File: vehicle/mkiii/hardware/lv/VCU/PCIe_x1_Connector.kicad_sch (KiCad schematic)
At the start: 15 parts, among them J2 J_PCIe_x1, U13 MCP6001T-I/LT

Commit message: Resolved some "footprint not exist" issues
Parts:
- J2: footprint OEM:J_PCIe_x1 -> OEM:J_PCIe_x1_Key
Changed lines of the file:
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@@
 			)
 		)
-		(property "Footprint" "OEM:J_PCIe_x1"
+		(property "Footprint" "OEM:J_PCIe_x1_Key"
 			(at 170.18 77.47 0)
 			(effects

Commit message: Layout completed, review required
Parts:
- renumbered C9 to C12, C30 to C13, C27 to C14, R45 to R11, R46 to R12, R42 to R13, R47 to R14, R48 to R15, R44 to R16, R43 to R17, U13 to U3
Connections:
- no-connect marks 15 -> 17
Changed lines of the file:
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@@
 	)
 	(no_connect
+		(at 187.96 134.62)
+	)
+	(no_connect
 		(at 190.5 91.44)
 	)
@@
 	)
 	(no_connect
+		(at 152.4 88.9)
+	)
+	(no_connect
 		(at 190.5 116.84)
 	)
@@
 		(dnp no)
 		(fields_autoplaced yes)
-		(property "Reference" "R42"
+		(property "Reference" "R13"
 			(at 203.2 38.0999 0)
 			(effects
@@
 			(project "VCU"
 				(path "/ec5dd9e3-3092-4af4-bee1-94131d9ab7f8/f5075997-e0a3-4d84-b3da-8739948f4d50"
-					(reference "R42")
+					(reference "R13")
 					(unit 1)
 				)
@@
 		(dnp no)
 		(fields_autoplaced yes)
-		(property "Reference" "R46"
+		(property "Reference" "R12"
 			(at 143.51 175.2599 0)
 			(effects
@@
 			(project "VCU"
 				(path "/ec5dd9e3-3092-4af4-bee1-94131d9ab7f8/f5075997-e0a3-4d84-b3da-8739948f4d50"
-					(reference "R46")
+					(reference "R12")
 					(unit 1)
 				)
@@
 		(dnp no)
 		(fields_autoplaced yes)
-		(property "Reference" "C27"
+		(property "Reference" "C14"
 			(at 213.36 29.21 90)
 			(effects
@@
 			(project "VCU"
 				(path "/ec5dd9e3-3092-4af4-bee1-94131d9ab7f8/f5075997-e0a3-4d84-b3da-8739948f4d50"
-					(reference "C27")
+					(reference "C14")
 					(unit 1)
 				)
@@
 		(dnp no)
 		(fields_autoplaced yes)
-		(property "Reference" "R48"
+		(property "Reference" "R15"
 			(at 220.98 90.1699 0)
 			(effects
@@
 			(project "VCU"
 				(path "/ec5dd9e3-3092-4af4-bee1-94131d9ab7f8/f5075997-e0a3-4d84-b3da-8739948f4d50"
-					(reference "R48")
+					(reference "R15")
 					(unit 1)
 				)
@@
 		(dnp no)
 		(fields_autoplaced yes)
-		(property "Reference" "C9"
+		(property "Reference" "C12"
 			(at 135.89 63.4999 0)
 			(effects
@@
 			(project ""
 				(path "/ec5dd9e3-3092-4af4-bee1-94131d9ab7f8/f5075997-e0a3-4d84-b3da-8739948f4d50"
-					(reference "C9")
+					(reference "C12")
 					(unit 1)
 				)
@@
 		(on_board yes)
 		(dnp no)
-		(property "Reference" "R44"
+		(property "Reference" "R16"
 			(at 236.22 63.4999 0)
 			(effects
@@
 			(project "VCU"
 				(path "/ec5dd9e3-3092-4af4-bee1-94131d9ab7f8/f5075997-e0a3-4d84-b3da-8739948f4d50"
-					(reference "R44")
+					(reference "R16")
 					(unit 1)
 				)
@@
 		(dnp no)
 		(fields_autoplaced yes)
-		(property "Reference" "C30"
+		(property "Reference" "C13"
 			(at 137.16 86.3599 0)
 			(effects
@@
 			(project "VCU"
 				(path "/ec5dd9e3-3092-4af4-bee1-94131d9ab7f8/f5075997-e0a3-4d84-b3da-8739948f4d50"
-					(reference "C30")
+					(reference "C13")
 					(unit 1)
 				)
@@
 		(dnp no)
 		(fields_autoplaced yes)
-		(property "Reference" "U13"
+		(property "Reference" "U3"
 			(at 223.52 43.1098 0)
 			(effects
@@
 			(project "VCU"
 				(path "/ec5dd9e3-3092-4af4-bee1-94131d9ab7f8/f5075997-e0a3-4d84-b3da-8739948f4d50"
-					(reference "U13")
+					(reference "U3")
 					(unit 1)
 				)
@@
 		(on_board yes)
 		(dnp no)
-		(property "Reference" "R47"
+		(property "Reference" "R14"
 			(at 220.98 80.0099 0)
 			(effects
@@
 			(project "VCU"
 				(path "/ec5dd9e3-3092-4af4-bee1-94131d9ab7f8/f5075997-e0a3-4d84-b3da-8739948f4d50"
-					(reference "R47")
+					(reference "R14")
 					(unit 1)
 				)
@@
 		(dnp no)
 		(fields_autoplaced yes)
-		(property "Reference" "R43"
+		(property "Reference" "R17"
 			(at 236.22 73.6599 0)
 			(effects
@@
 			(project "VCU"
 				(path "/ec5dd9e3-3092-4af4-bee1-94131d9ab7f8/f5075997-e0a3-4d84-b3da-8739948f4d50"
-					(reference "R43")
+					(reference "R17")
 					(unit 1)
 				)
@@
 		(dnp no)
 		(fields_autoplaced yes)
-		(property "Reference" "R45"
+		(property "Reference" "R11"
 			(at 124.46 175.2599 0)
 			(effects
@@
 			(project "VCU"
 				(path "/ec5dd9e3-3092-4af4-bee1-94131d9ab7f8/f5075997-e0a3-4d84-b3da-8739948f4d50"
-					(reference "R45")
+					(reference "R11")
 					(unit 1)
 				)

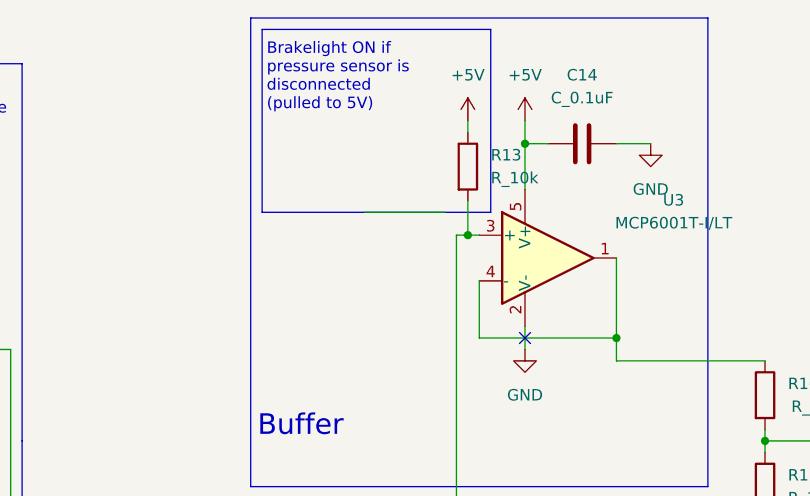
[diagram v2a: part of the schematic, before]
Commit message: Minor ERC Fixes in Schematics; Minor Silkscreen Changes; Addedc Subteam Layout; Added Production Files.
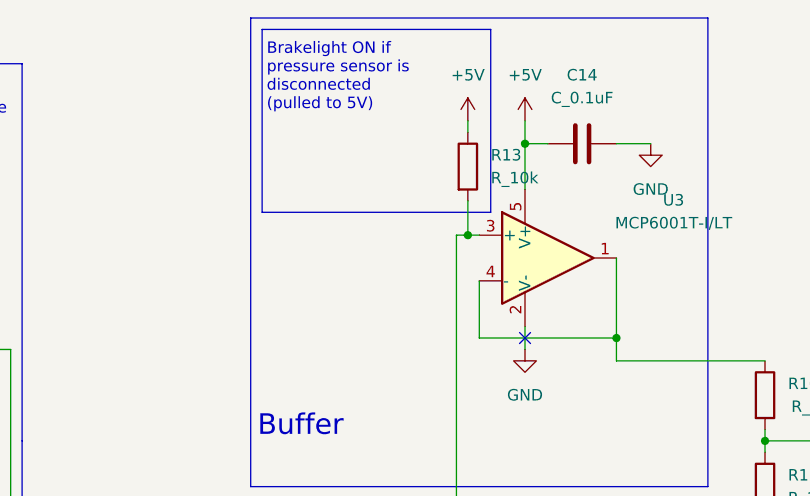
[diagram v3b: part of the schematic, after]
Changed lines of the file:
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@@
-		)
-	)
-	(wire
-		(pts
-			(xy 198.12 44.45) (xy 189.23 44.45)
-		)
-		(stroke
-			(width 0)
-			(type default)
 		)
 	)
@@
 		(dnp no)
 		(fields_autoplaced yes)
-		(property "Reference" "#PWR?"
+		(property "Reference" "#PWR0151"
 			(at 207.01 38.1 0)
 			(effects
@@
 			(project ""
 				(path "/ec5dd9e3-3092-4af4-bee1-94131d9ab7f8/f5075997-e0a3-4d84-b3da-8739948f4d50"
-					(reference "#PWR?")
+					(reference "#PWR0151")
 					(unit 1)
 				)
@@
 		(on_board yes)
 		(dnp no)
-		(property "Reference" "#PWR?"
+		(property "Reference" "#PWR0138"
 			(at 115.57 110.49 0)
 			(effects
@@
 			(project "VCU"
 				(path "/ec5dd9e3-3092-4af4-bee1-94131d9ab7f8/f5075997-e0a3-4d84-b3da-8739948f4d50"
-					(reference "#PWR?")
+					(reference "#PWR0138")
 					(unit 1)
 				)
@@
 		(on_board yes)
 		(dnp no)
-		(property "Reference" "#PWR?"
+		(property "Reference" "#PWR0137"
 			(at 118.11 82.55 0)
 			(effects
@@
 			(project ""
 				(path "/ec5dd9e3-3092-4af4-bee1-94131d9ab7f8/f5075997-e0a3-4d84-b3da-8739948f4d50"
-					(reference "#PWR?")
+					(reference "#PWR0137")
 					(unit 1)
 				)
@@
 		(dnp no)
 		(fields_autoplaced yes)
-		(property "Reference" "#PWR?"
+		(property "Reference" "#PWR0142"
 			(at 140.97 175.26 0)
 			(effects
@@
 			(project ""
 				(path "/ec5dd9e3-3092-4af4-bee1-94131d9ab7f8/f5075997-e0a3-4d84-b3da-8739948f4d50"
-					(reference "#PWR?")
+					(reference "#PWR0142")
 					(unit 1)
 				)
@@
 		(dnp no)
 		(fields_autoplaced yes)
-		(property "Reference" "#PWR?"
+		(property "Reference" "#PWR0147"
 			(at 207.01 66.04 0)
 			(effects
@@
 			(project "VCU"
 				(path "/ec5dd9e3-3092-4af4-bee1-94131d9ab7f8/f5075997-e0a3-4d84-b3da-8739948f4d50"
-					(reference "#PWR?")
+					(reference "#PWR0147")
 					(unit 1)
 				)
@@
 		(dnp no)
 		(fields_autoplaced yes)
-		(property "Reference" "#PWR?"
+		(property "Reference" "#PWR0141"
 			(at 132.08 74.93 0)
 			(effects
@@
 			(project "VCU"
 				(path "/ec5dd9e3-3092-4af4-bee1-94131d9ab7f8/f5075997-e0a3-4d84-b3da-8739948f4d50"
-					(reference "#PWR?")
+					(reference "#PWR0141")
 					(unit 1)
 				)
@@
 		(dnp no)
 		(fields_autoplaced yes)
-		(property "Reference" "#PWR?"
+		(property "Reference" "#PWR0150"
 			(at 233.68 85.09 0)
 			(effects
@@
 			(project "VCU"
 				(path "/ec5dd9e3-3092-4af4-bee1-94131d9ab7f8/f5075997-e0a3-4d84-b3da-8739948f4d50"
-					(reference "#PWR?")
+					(reference "#PWR0150")
 					(unit 1)
 				)
@@
 		(dnp no)
 		(fields_autoplaced yes)
-		(property "Reference" "#PWR?"
+		(property "Reference" "#PWR0145"
 			(at 218.44 101.6 0)
 			(effects
@@
 			(project "VCU"
 				(path "/ec5dd9e3-3092-4af4-bee1-94131d9ab7f8/f5075997-e0a3-4d84-b3da-8739948f4d50"
-					(reference "#PWR?")
+					(reference "#PWR0145")
 					(unit 1)
 				)
@@
 		(on_board yes)
 		(dnp no)
-		(property "Reference" "#PWR?"
+		(property "Reference" "#PWR0140"
 			(at 118.11 97.79 0)
 			(effects
@@
 			(project ""
 				(path "/ec5dd9e3-3092-4af4-bee1-94131d9ab7f8/f5075997-e0a3-4d84-b3da-8739948f4d50"
-					(reference "#PWR?")
+					(reference "#PWR0140")
 					(unit 1)
 				)
@@
 		(dnp no)
 		(fields_autoplaced yes)
-		(property "Reference" "#PWR?"
+		(property "Reference" "#PWR0149"
 			(at 200.66 38.1 0)
 			(effects
@@
 			(project ""
 				(path "/ec5dd9e3-3092-4af4-bee1-94131d9ab7f8/f5075997-e0a3-4d84-b3da-8739948f4d50"
-					(reference "#PWR?")
+					(reference "#PWR0149")
 					(unit 1)
 				)
@@
 		(dnp no)
 		(fields_autoplaced yes)
-		(property "Reference" "#PWR?"
+		(property "Reference" "#PWR0144"
 			(at 190.5 152.4 0)
 			(effects
@@
 			(project "VCU"
 				(path "/ec5dd9e3-3092-4af4-bee1-94131d9ab7f8/f5075997-e0a3-4d84-b3da-8739948f4d50"
-					(reference "#PWR?")
+					(reference "#PWR0144")
 					(unit 1)
 				)
@@
 		(dnp no)
 		(fields_autoplaced yes)
-		(property "Reference" "#PWR?"
+		(property "Reference" "#PWR0143"
 			(at 121.92 175.26 0)
 			(effects
@@
 			(project ""
 				(path "/ec5dd9e3-3092-4af4-bee1-94131d9ab7f8/f5075997-e0a3-4d84-b3da-8739948f4d50"
-					(reference "#PWR?")
+					(reference "#PWR0143")
 					(unit 1)
 				)
@@
 		(dnp no)
 		(fields_autoplaced yes)
-		(property "Reference" "#PWR?"
+		(property "Reference" "#PWR0139"
 			(at 133.35 97.79 0)
 			(effects
@@
 			(project "VCU"
 				(path "/ec5dd9e3-3092-4af4-bee1-94131d9ab7f8/f5075997-e0a3-4d84-b3da-8739948f4d50"
-					(reference "#PWR?")
+					(reference "#PWR0139")
 					(unit 1)
 				)
@@
 		(dnp no)
 		(fields_autoplaced yes)
-		(property "Reference" "#PWR?"
+		(property "Reference" "#PWR0148"
 			(at 220.98 43.18 0)
 			(effects
@@
 			(project "VCU"
 				(path "/ec5dd9e3-3092-4af4-bee1-94131d9ab7f8/f5075997-e0a3-4d84-b3da-8739948f4d50"
-					(reference "#PWR?")
+					(reference "#PWR0148")
 					(unit 1)
 				)
@@
 		(dnp no)
 		(fields_autoplaced yes)
-		(property "Reference" "#PWR?"
+		(property "Reference" "#PWR0146"
 			(at 234.95 139.7 0)
 			(effects
@@
 			(project "VCU"
 				(path "/ec5dd9e3-3092-4af4-bee1-94131d9ab7f8/f5075997-e0a3-4d84-b3da-8739948f4d50"
-					(reference "#PWR?")
-					(unit 1)
-				)
+					(reference "#PWR0146")
+					(unit 1)
+				)
